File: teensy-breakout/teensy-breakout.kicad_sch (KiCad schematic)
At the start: 1 part, among them U1 Teensy4.1

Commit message: Initial work on teensy brakeout PCB
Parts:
- added C1, C2: 100u, symbol Device:C_Polarized_US
- added C10, C11: C, symbol Device:C
- added C12, C9: 100n, Capacitor_SMD:C_0805_2012Metric, symbol Device:C
- added C13, C3, C5, C7, C8: 10u, Capacitor_SMD:C_0805_2012Metric, symbol Device:C
- added C4, C6: 1u, Capacitor_SMD:C_0805_2012Metric, symbol Device:C
- added CR1: L7805CD2T-TR, Custom:D2PAKSMD_2L_STD-ST_STM, symbol custom:L7805CD2T-TR
- added CR2: MBRD10100CT-13, Custom:TO252DPAK_DIO, symbol custom:MBRD10100CT-13
- added D1, D2: LED, symbol Device:LED
- added J1: USB_B, Connector_USB:USB_B_OST_USB-B1HSxx_Horizontal, symbol Connector:USB_B
- added Q1: IRL530NSTRLPBF, Custom:D2PAKSMD_2L_STD-ST_STM, symbol custom:IRL530NSTRLPBF
- added R1: 1k, Resistor_SMD:R_0805_2012Metric, symbol Device:R_US
- added R2: 10k, Resistor_SMD:R_0805_2012Metric, symbol Device:R_US
- added R3, R4: 270, Resistor_SMD:R_0805_2012Metric, symbol Device:R_US
- added R5, R6: 2k, Resistor_SMD:R_0805_2012Metric, symbol Device:R_US
- added U2: ~, Custom:BNO085, symbol custom:BNO085
- added U3: FT232RL, Package_SO:SSOP-28_5.3x10.2mm_P0.65mm, symbol Interface_USB:FT232RL
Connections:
- net GND: now reaches U1.1 (GND)
- net GND: now also U1.34 (GND), U1.47 (GND), C1.2, C10.2, C11.2, C12.2, C13.2, C2.2, C3.2, C4.2, C5.2, C6.2, C7.2, C8.2, C9.1, CR1.2 (GROUND), J1.4 (GND), J1.5 (Shield), Q1.3 (S), R2.1, U2.3 (GND), U3.18 (GND), U3.21 (GND), U3.25 (AGND), U3.26 (TEST), U3.7 (GND)
- net +3V3: now reaches U1.15 (3V3)
- net +3V3: now also U1.46 (3V3), C11.1, C7.1, R5.1, R6.1, U2.1 (VIN)
- net UART1 RX: now reaches U1.2 (0_RX1_CRX2_CS1)
- net UART1 RX: now also U3.1 (TXD)
- net UART1 TX: now reaches U1.3 (1_TX1_CTX2_MISO1)
- net UART1 TX: now also U3.5 (RXD)
- net UART1 RTS: now reaches U1.4 (2_OUT2)
- net UART1 RTS: now also U3.3 (RTS)
- net I2C0_SDA: now reaches U1.40 (18_A4_SDA)
- net I2C0_SDA: now also R6.2, U2.5 (SDA)
- net I2C0_SCL: now reaches U1.41 (19_A5_SCL)
- net I2C0_SCL: now also R5.2, U2.4 (SCL)
- net +5V: now reaches U1.48 (VIN)
- net +5V: now also C10.1, C12.1, C13.1, C2.1, C5.1, C6.1, C8.1, CR1.3 (OUTPUT), U3.19 (~{RESET}), U3.20 (VCC)
- net UART1 CTS: now reaches U1.5 (3_LRCLK2)
- net UART1 CTS: now also U3.11 (CTS)
- new net: CR2.1, CR2.3, Q1.2 (D)
- new net: D1.1 (K), U3.23 (CBUS0)
- new net: D1.2 (A), R3.2
- new net: Q1.1 (G), R1.2, R2.2
- new net: C9.2, R3.1, R4.1, U3.17 (3V3OUT), U3.4 (VCCIO)
- new net: D2.1 (K), U3.22 (CBUS1)
- new net: D2.2 (A), R4.2
- new net +12V: C1.1, C3.1, C4.1, CR1.1 (INPUT), CR2.2
- new net USB_DM: J1.2 (D-)
- new net USB_DP: J1.3 (D+)
- no-connect marks 0 -> 18
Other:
- moved on the sheet: U1

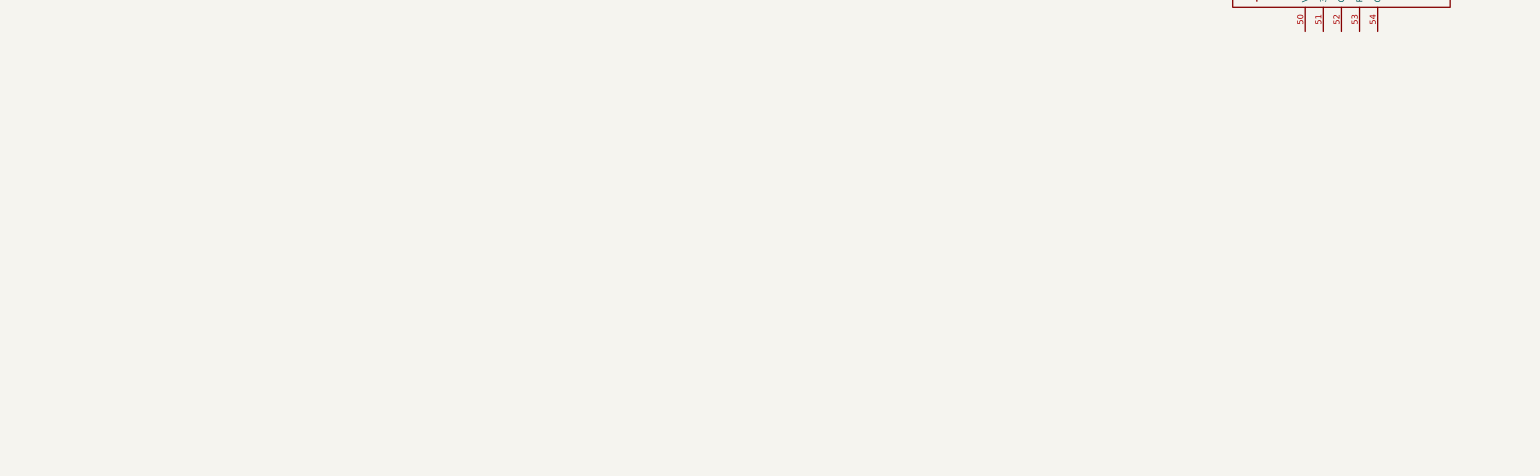
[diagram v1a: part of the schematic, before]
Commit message: Started working to integrate ZED-F9P and feather. Still need to make Zed-F9P footprint.
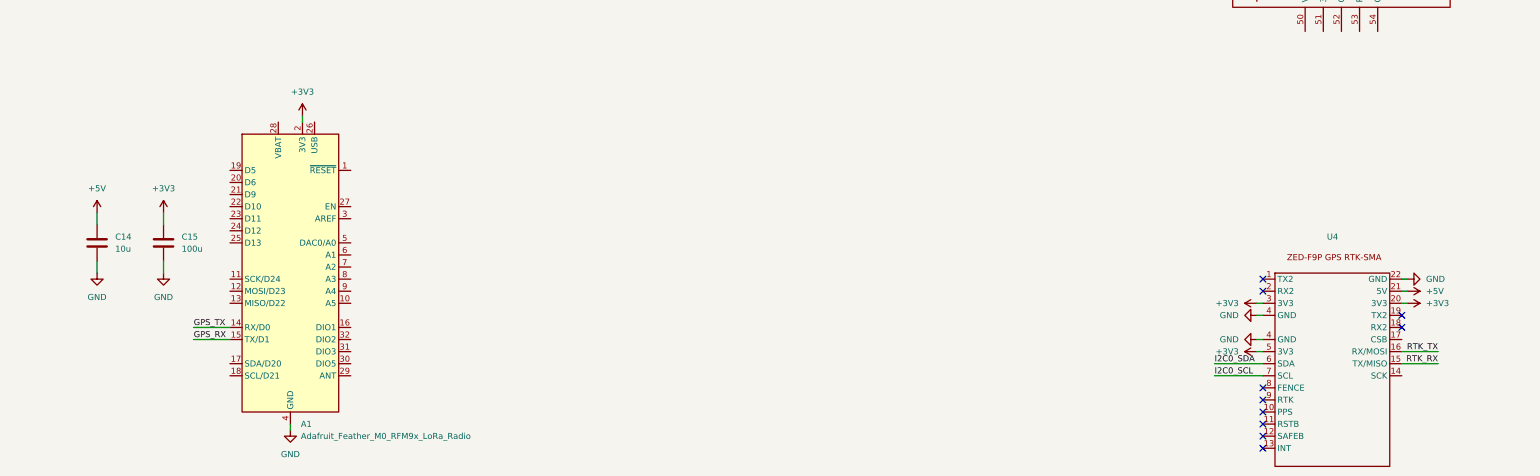
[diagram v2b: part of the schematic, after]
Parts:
- added A1: Adafruit_Feather_M0_RFM9x_LoRa_Radio, Module:Adafruit_Feather_M0_RFM, symbol MCU_Module:Adafruit_Feather_M0_RFM9x_LoRa_Radio
- added C14: 10u, symbol Device:C
- added C15: 100u, symbol Device:C
- added U4: ~, symbol custom:ZED-F9P-GPS-RTK-SMA
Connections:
- net +3V3: now also A1.2 (3V3), C15.2, U4.20 (3V3), U4.3 (3V3), U4.5 (3V3)
- net +5V: now also C14.1, U4.21 (5V)
- net GND: now also A1.4 (GND), C14.2, C15.1, U4.22 (GND), U4.4 (GND)
- net I2C0_SCL: now also U4.7 (SCL)
- net I2C0_SDA: now also U4.6 (SDA)
- new net GPS_RX: A1.15 (TX/D1)
- new net GPS_TX: A1.14 (RX/D0)
- new net RTK_RX: U4.15 (TX/MISO)
- new net RTK_TX: U4.16 (RX/MOSI)
- no-connect marks 18 -> 28

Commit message: More work done on schematic, seems good to me
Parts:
- added C16, C21, C23, C24: 10u, Capacitor_SMD:C_0805_2012Metric_Pad1.18x1.45mm_HandSolder, symbol Device:C
- added C17, C18, C19, C22: 1u, Capacitor_SMD:C_0805_2012Metric_Pad1.18x1.45mm_HandSolder, symbol Device:C
- added C20: 100u, Capacitor_SMD:C_0805_2012Metric_Pad1.18x1.45mm_HandSolder, symbol Device:C
- added D3: LED, LED_SMD:LED_0805_2012Metric_Pad1.15x1.40mm_HandSolder, symbol Device:LED
- added J10, J15, J16, J2, J3, J4, J5, J6, J7: 1988820, Custom:CONN_1988820, symbol custom:1988820
- added J11, J12, J13, J14, J18: 1988817, Custom:CONN_1988817, symbol custom:1988817
- added J17, J21, J9: 1988956, Custom:CONN_1988956, symbol custom:1988956
- added J19, J20: 1989010, Custom:PHOENIX_1989010, symbol custom:1989010
- added J8: 1988833, Custom:CONN_1988833, symbol custom:1988833
- added R10, R9: 10k, Resistor_SMD:R_0805_2012Metric_Pad1.20x1.40mm_HandSolder, symbol Device:R_US
- added R11, R12: 2k, Resistor_SMD:R_0805_2012Metric_Pad1.20x1.40mm_HandSolder, symbol Device:R_US
- added R7: R_US, symbol Device:R_US
- added R8: 1k, Resistor_SMD:R_0805_2012Metric_Pad1.20x1.40mm_HandSolder, symbol Device:R_US
- added SW1: 7101MD9AQE, Custom:SW3_7101MD9AQE_CNK, symbol custom:7101MD9AQE
- added U10, U7: LSF0102DCUR, DCU0008A_N, symbol custom:LSF0102DCUR
- added U5: ~, Custom:RFM69HCW Adafruit Breakout, symbol custom:RFM69HCW_Adafruit_Breakout
- added U6: ICL7667CBAZA-TDKR, Custom:SOIC8_4X5_INR, symbol custom:ICL7667CBAZA-TDKR
- added U9: ICL7667CBAZA-TDKR, Custom:DCU0008A_M, symbol custom:ICL7667CBAZA-TDKR
- C12: value 100n -> 1u; footprint Capacitor_SMD:C_0805_2012Metric -> Capacitor_SMD:C_0805_2012Metric_Pad1.18x1.45mm_HandSolder
- C13, C3, C4, C5, C6, C7, C8, C9: footprint Capacitor_SMD:C_0805_2012Metric -> Capacitor_SMD:C_0805_2012Metric_Pad1.18x1.45mm_HandSolder
- C14: footprint (none) -> Capacitor_SMD:C_0805_2012Metric_Pad1.18x1.45mm_HandSolder
- C15: value 100u -> 1u; footprint (none) -> Capacitor_SMD:C_0805_2012Metric_Pad1.18x1.45mm_HandSolder
- R3, R4, R5, R6: footprint Resistor_SMD:R_0805_2012Metric -> Resistor_SMD:R_0805_2012Metric_Pad1.20x1.40mm_HandSolder
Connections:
- net RTK_RX is gone; now on net GPS_TX: U4.15 (TX/MISO)
- net RTK_TX is gone; now on net GPS_RX: U4.16 (RX/MOSI)
- net +12V: now also J9.2, R8.1
- net +3V3: now also C14.1, C17.2, C19.1, C20.1, C21.1, C22.1, C24.1, J16.1, J4.1, J4.2, J4.3, J4.4, J5.1, J5.2, J5.3, J5.4, R10.1, R11.1, R12.1, R7.2, R9.1, U10.2 (VREF_A), U5.1 (VIN), U7.2 (VREF_A), U9.3 (V-)
- net +5V: now also C16.1, C18.1, C23.1, J11.1, J12.1, J13.1, J14.1, J15.1, J6.1, J6.2, J6.3, J6.4, J7.1, J7.2, J7.3, J7.4, J8.4, J8.5, SW1.1, U10.7 (VREF_B), U10.8 (EN), U6.6 (V+), U7.7 (VREF_B), U7.8 (EN), U9.6 (V+); no longer C14.1, CR1.3 (OUTPUT)
- net GND: now also C16.2, C17.1, C18.2, C19.2, C20.2, C21.2, C22.2, C23.2, C24.2, J10.1, J10.2, J11.3, J12.3, J13.3, J14.3, J15.4, J16.4, J2.1, J2.2, J2.3, J2.4, J3.1, J3.2, J3.3, J3.4, U10.1 (GND), U5.2 (GND), U6.3 (V-), U7.1 (GND)
- net at CR2.1, CR2.3, Q1.2 (D): now also D3.1 (K), J9.1
- net BRAKE: now reaches R1.1
- net BRAKE: now also U1.18 (26_A12_MOSI1)
- net RC_TX: now reaches U1.10 (8_TX2_IN1)
- net RC_TX: now also U9.4 (INB)
- net NP4: now reaches U1.11 (9_OUT1C)
- net NP4: now also U7.4 (A2)
- net RF_CS: now reaches U1.12 (10_CS_MQSR)
- net RF_CS: now also U5.8 (CS)
- net MOSI: now reaches U1.13 (11_MOSI_CTX1)
- net MOSI: now also J18.1, U5.7 (MOSI)
- net MISO: now reaches U1.14 (12_MISO_MQSL)
- net MISO: now also J18.2, U5.6 (MISO)
- net J0_1: now reaches U1.16 (24_A10_TX6_SCL2)
- net J0_1: now also J19.1
- net J0_2: now reaches U1.17 (25_A11_RX6_SDA2)
- net J0_2: now also J19.2
- net PUL: now reaches U1.19 (27_A13_SCK1)
- net PUL: now also J16.2, U6.2 (INA)
- net J0_3: now reaches U1.20 (28_RX7)
- net J0_3: now also J19.3
- net J0_4: now reaches U1.21 (29_TX7)
- net J0_4: now also J19.4
- net J0_5: now reaches U1.22 (30_CRX3)
- net J0_5: now also J19.5
- net J0_6: now reaches U1.23 (31_CTX3)
- net J0_6: now also J19.6
- net J0_7: now reaches U1.24 (32_OUT1B)
- net J0_7: now also J19.7
- net J0_8: now reaches U1.25 (33_MCLK2)
- net J0_8: now also J19.8
- net J1_1: now reaches U1.26 (34_RX8)
- net J1_1: now also J20.1
- net J1_2: now reaches U1.27 (35_TX8)
- net J1_2: now also J20.2
- net RF_G0: now reaches U1.28 (36_CS)
- net RF_G0: now also U5.4 (G0)
- net RF_RST: now reaches U1.29 (37_CS)
- net RF_RST: now also U5.9 (RST)
- net DIR: now reaches U1.30 (38_CS1_IN1)
- net DIR: now also J16.3, U6.4 (INB)
- net ALM: now reaches U1.31 (39_MISO1_OUT1A)
- net ALM: now also J8.1, R7.1
- net J1_3: now reaches U1.32 (40_A16)
- net J1_3: now also J20.3
- net J1_4: now reaches U1.33 (41_A17)
- net J1_4: now also J20.4
- net SCK: now reaches U1.35 (13_SCK_LED)
- net SCK: now also J18.3, U5.5 (SCK)
- net J1_5: now reaches U1.36 (14_A0_TX3_SPDIF_OUT)
- net J1_5: now also J20.5
- net J1_6: now reaches U1.37 (15_A1_RX3_SPDIF_IN)
- net J1_6: now also J20.6
- net at U1.38 (16_A2_RX4_SCL1): now also J17.2, R12.2
- net at U1.39 (17_A3_TX4_SDA1): now also J17.1, R11.2
- net J1_7: now reaches U1.42 (20_A6_TX5_LRCLK1)
- net J1_7: now also J20.7
- net J1_8: now reaches U1.43 (21_A7_RX5_BCLK1)
- net J1_8: now also J20.8
- net J2_1: now reaches U1.44 (22_A8_CTX1)
- net J2_1: now also J21.1
- net J2_2: now reaches U1.45 (23_A9_CRX1_MCLK1)
- net J2_2: now also J21.2
- net NP1: now reaches U1.6 (4_BCLK2)
- net NP1: now also U10.3 (A1)
- net NP2: now reaches U1.7 (5_IN2)
- net NP2: now also U10.4 (A2)
- net NP3: now reaches U1.8 (6_OUT1D)
- net NP3: now also U7.3 (A1)
- net RC_RX: now reaches U1.9 (7_RX2_OUT1A)
- net RC_RX: now also U9.2 (INA)
- new net: D3.2 (A), R8.2
- new net: J11.2, U10.6 (B1)
- new net: J15.2, U9.7 (OUTA)
- new net: J15.3, U9.5 (OUTB)
- new net: J13.2, U7.6 (B1)
- new net: J12.2, U10.5 (B2)
- new net: CR1.3 (OUTPUT), SW1.2
- new net: J14.2, U7.5 (B2)
- new net DIR_MIN: J8.2, U6.5 (OUTB)
- new net LIM_L: J10.4, R9.2
- new net LIM_R: J10.3, R10.2
- new net PUL_MIN: J8.3, U6.7 (OUTA)
- no-connect marks 28 -> 32

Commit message: Forgot to add power LED
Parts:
- added D4: LED, symbol Device:LED
- added R13: R_US, symbol Device:R_US
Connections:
- net +5V: now also D4.2 (A)
- net GND: now also R13.2
- new net: D4.1 (K), R13.1

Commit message: Work on layout & wiring. Mostly done, need to look it over. It's very messy :(
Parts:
- removed J16: 1988820, Custom:CONN_1988820, symbol custom:1988820
- removed U9: ICL7667CBAZA-TDKR, Custom:DCU0008A_M, symbol custom:ICL7667CBAZA-TDKR
- added C25: 1u, Capacitor_SMD:C_0805_2012Metric_Pad1.18x1.45mm_HandSolder, symbol Device:C
- added CR3, CR4: L7805CD2T-TR, Custom:D2PAKSMD_2L_STD-ST_STM, symbol custom:L7805CD2T-TR
- added J22: 1988817, Custom:CONN_1988817, symbol custom:1988817
- added R14, R15, R16: 200k, Resistor_SMD:R_0805_2012Metric_Pad1.20x1.40mm_HandSolder, symbol Device:R_US
- added U8: LSF0102DCUR, Custom:DCU0008A_M, symbol custom:LSF0102DCUR
- C1, C2: footprint (none) -> Custom:CAP_A765EB_KEM
- C20: value 100u -> 1u
- D1, D2: value LED -> BLUE; footprint (none) -> LED_SMD:LED_0805_2012Metric
- D4: value LED -> GREEN; footprint (none) -> LED_SMD:LED_0805_2012Metric
- R13: value R_US -> 120; footprint (none) -> Resistor_SMD:R_0805_2012Metric_Pad1.20x1.40mm_HandSolder
- R7: value R_US -> 500; footprint (none) -> Resistor_SMD:R_0805_2012Metric_Pad1.20x1.40mm_HandSolder
- U10, U7: footprint DCU0008A_N -> Custom:DCU0008A_M
- U4: footprint (none) -> Custom:ZED F9P RTK SMA
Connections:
- net +12V: now also J21.1, CR3.1 (INPUT), CR4.1 (INPUT)
- net +3V3: now also C16.1, U4.21 (3V3), U4.6 (3V3), U8.2 (VREF_A); no longer U4.20 (3V3), U4.5 (3V3)
- net +5V: now also U4.22 (5V), C25.1, R14.1; no longer C16.1, J11.1, J12.1, J13.1, J14.1, J6.1, J6.2, J6.3, J6.4, J7.1, J7.2, J7.3, J7.4, U10.7 (VREF_B), U10.8 (EN), U4.21 (5V), U7.7 (VREF_B), U7.8 (EN)
- net ALM: now also U1.43 (21_A7_RX5_BCLK1); no longer U1.31 (39_MISO1_OUT1A)
- net BRAKE: now also U1.44 (22_A8_CTX1); no longer U1.18 (26_A12_MOSI1)
- net GND: now also J21.2, U4.23 (GND), U4.5 (GND), C25.2, CR3.2 (GROUND), CR4.2 (GROUND), U8.1 (GND); no longer U4.22 (GND)
- net GPS_RX: now also U4.17 (RX/MOSI); no longer U4.16 (RX/MOSI)
- net GPS_TX: now also U4.16 (TX/MISO); no longer U4.15 (TX/MISO)
- net I2C0_SCL: now also U4.8 (SCL); no longer U4.7 (SCL)
- net I2C0_SDA: now also U4.7 (SDA); no longer U4.6 (SDA)
- net PUL: now also U1.45 (23_A9_CRX1_MCLK1); no longer U1.19 (27_A13_SCK1)
- net RC_RX: now also U8.3 (A1)
- net RC_TX: now also U8.4 (A2)
- net USB_DM: now also U3.16 (USBD-)
- net USB_DP: now also U3.15 (USBD+)
- net at J15.2: now also U8.6 (B1)
- net at J15.3: now also U8.5 (B2)
- net J1_8: no longer names the net of J20.8
- net J1_8: no longer U1.43 (21_A7_RX5_BCLK1)
- removed net J2_1: J21.1, U1.44 (22_A8_CTX1)
- removed net J2_2: J21.2, U1.45 (23_A9_CRX1_MCLK1)
- net MISO renamed MISO0
- net MOSI renamed MOSI0
- net SCK renamed SCK0
- new net: CR4.3 (OUTPUT), J11.1, J12.1, J13.1, J14.1, R15.1, R16.1
- new net: CR3.3 (OUTPUT), J6.1, J6.2, J6.3, J6.4, J7.1, J7.2, J7.3, J7.4
- new net: R16.2, U7.7 (VREF_B), U7.8 (EN)
- new net: R15.2, U10.7 (VREF_B), U10.8 (EN)
- new net: R14.2, U8.7 (VREF_B), U8.8 (EN)
- new net MISO1: J22.2, U1.31 (39_MISO1_OUT1A)
- new net MOSI1: J22.1, U1.18 (26_A12_MOSI1)
- new net SCK1: J22.3, U1.19 (27_A13_SCK1)
- no-connect marks 32 -> 83
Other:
- moved on the sheet: J6, J7

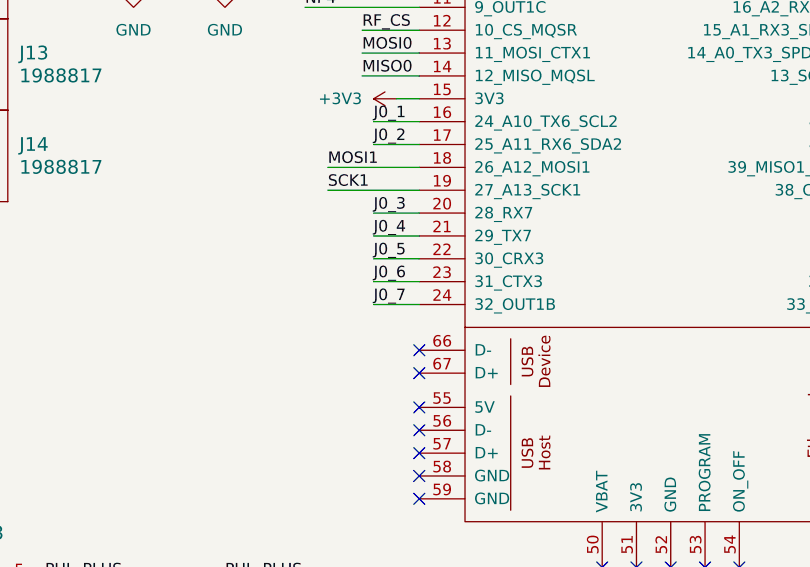
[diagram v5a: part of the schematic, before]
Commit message: Added connection for limit switches, started work on adding headers
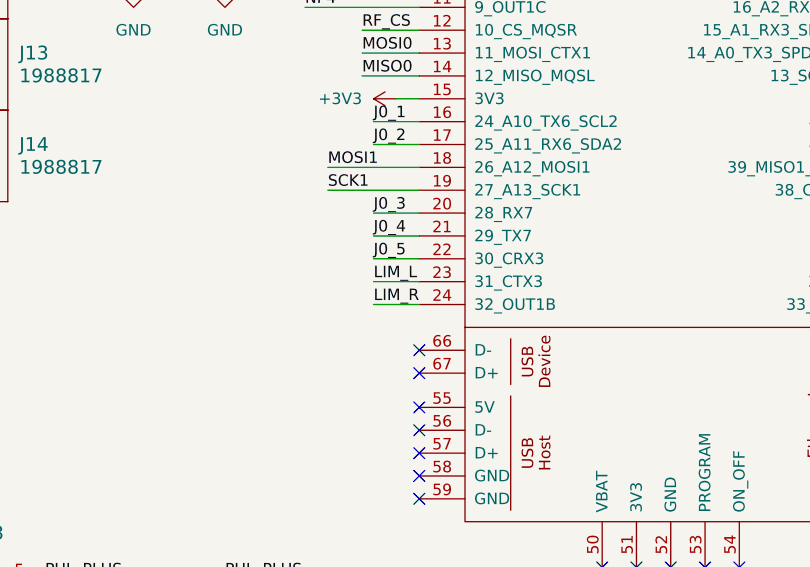
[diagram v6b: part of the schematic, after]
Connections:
- net J0_6: no longer U1.23 (31_CTX3)
- net J0_7: no longer U1.24 (32_OUT1B)
- net LIM_L: now also U1.23 (31_CTX3)
- net LIM_R: now also U1.24 (32_OUT1B)
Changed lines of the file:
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@@
 		)
 	)
-	(label "J0_6"
+	(label "LIM_L"
 		(at 402.59 100.33 0)
 		(fields_autoplaced yes)
@@
 		)
 	)
-	(label "J0_7"
+	(label "LIM_R"
 		(at 402.59 102.87 0)
 		(fields_autoplaced yes)

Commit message: Improved schematic layout, still in  progress
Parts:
- removed C10, C11: C, symbol Device:C
- removed CR1, CR3, CR4: L7805CD2T-TR, Custom:D2PAKSMD_2L_STD-ST_STM, symbol custom:L7805CD2T-TR
- removed J10, J15, J2, J3, J4, J5, J6, J7: 1988820, Custom:CONN_1988820, symbol custom:1988820
- removed J11, J12, J13, J14, J18, J22: 1988817, Custom:CONN_1988817, symbol custom:1988817
- removed J17, J21, J9: 1988956, Custom:CONN_1988956, symbol custom:1988956
- removed J19, J20: 1989010, Custom:PHOENIX_1989010, symbol custom:1989010
- removed J8: 1988833, Custom:CONN_1988833, symbol custom:1988833
- added J10, J11, J14, J15, J4, J5, J6, J7, J8, J9: Conn_01x04, symbol Connector_Generic:Conn_01x04
- added J12: Conn_01x05, symbol Connector_Generic:Conn_01x05
- added J13, J19, J20, J21, J22: Conn_01x03, symbol Connector_Generic:Conn_01x03
- added J16: 1988956, Custom:CONN_1988956, symbol custom:1988956
- added J17, J18: Conn_01x08, symbol Connector_Generic:Conn_01x08
- added J2, J3: Conn_01x02, symbol Connector_Generic:Conn_01x02
- added R17: 1k, Resistor_SMD:R_0805_2012Metric_Pad1.20x1.40mm_HandSolder, symbol Device:R_US
- added U9: ~, symbol custom:D36V50Fx
- CR2: footprint Custom:TO252DPAK_DIO -> TO252DPAK_DIO
- Q1: footprint Custom:D2PAKSMD_2L_STD-ST_STM -> IRL530NSTRLPBF_INF
- U10, U7, U8: footprint Custom:DCU0008A_M -> DCU0008A_N
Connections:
- net J0_8 is gone; now on net J0_6: U1.25 (33_MCLK2)
- net +12V: now also R17.1, U9.11 (VRP), U9.5 (VRP)
- net +3V3: now also J17.7 (Pin_7), J6.1 (Pin_1), J6.2 (Pin_2), J6.3 (Pin_3), J6.4 (Pin_4), J7.1 (Pin_1), J7.2 (Pin_2), J7.3 (Pin_3), J7.4 (Pin_4)
- net +5V: now also R16.1, J10.1 (Pin_1), J12.4 (Pin_4), J12.5 (Pin_5), J19.1 (Pin_1), J20.1 (Pin_1), J21.1 (Pin_1), J22.1 (Pin_1), J8.1 (Pin_1), J8.2 (Pin_2), J8.3 (Pin_3), J8.4 (Pin_4), J9.1 (Pin_1), J9.2 (Pin_2), J9.3 (Pin_3), J9.4 (Pin_4)
- net ALM: now also J12.1 (Pin_1)
- net DIR_MIN: now also J12.2 (Pin_2)
- net GND: now also J10.4 (Pin_4), J11.1 (Pin_1), J11.2 (Pin_2), J13.3 (Pin_3), J14.4 (Pin_4), J15.4 (Pin_4), J17.8 (Pin_8), J18.8 (Pin_8), J19.3 (Pin_3), J20.3 (Pin_3), J21.3 (Pin_3), J22.3 (Pin_3), J4.1 (Pin_1), J4.2 (Pin_2), J4.3 (Pin_3), J4.4 (Pin_4), J5.1 (Pin_1), J5.2 (Pin_2), J5.3 (Pin_3), J5.4 (Pin_4), U9.2 (GND), U9.3 (GND), U9.8 (GND), U9.9 (GND)
- net J0_1: now also J17.1 (Pin_1)
- net J0_2: now also J17.2 (Pin_2)
- net J0_3: now also J17.3 (Pin_3)
- net J0_4: now also J17.4 (Pin_4)
- net J0_5: now also J17.5 (Pin_5)
- net J0_6: now also J17.6 (Pin_6)
- net J1_1: now also J18.1 (Pin_1)
- net J1_2: now also J18.2 (Pin_2)
- net J1_3: now also J18.3 (Pin_3)
- net J1_4: now also J18.4 (Pin_4)
- net J1_5: now also J18.5 (Pin_5)
- net J1_6: now also J18.6 (Pin_6)
- net J1_7: now also J18.7 (Pin_7)
- net LIM_L: now also J11.4 (Pin_4)
- net LIM_R: now also J11.3 (Pin_3)
- net MISO0: now also J14.2 (Pin_2)
- net MISO1: now also J15.2 (Pin_2)
- net MOSI0: now also J14.1 (Pin_1)
- net MOSI1: now also J15.1 (Pin_1)
- net PUL_MIN: now also J12.3 (Pin_3)
- net SCK0: now also J14.3 (Pin_3)
- net SCK1: now also J15.3 (Pin_3)
- net at CR2.1, CR2.3, D3.1 (K)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: now also J16.2
- net at R15.1: no longer R16.1
- net NP1_5V: now reaches U10.6 (B1)
- net NP1_5V: now also J19.2 (Pin_2)
- net at U8.6 (B1): now also J10.2 (Pin_2)
- net at U8.5 (B2): now also J10.3 (Pin_3)
- net I2C1_SDA: now reaches R11.2, U1.39 (17_A3_TX4_SDA1)
- net I2C1_SDA: now also J13.1 (Pin_1)
- net NP3_5V: now reaches U7.6 (B1)
- net NP3_5V: now also J21.2 (Pin_2)
- net NP2_5V: now reaches U10.5 (B2)
- net NP2_5V: now also J20.2 (Pin_2)
- net at SW1.2: now also U9.1 (VOUT), U9.7 (VOUT)
- net I2C1_SCL: now reaches R12.2, U1.38 (16_A2_RX4_SCL1)
- net I2C1_SCL: now also J13.2 (Pin_2)
- net NP4_5V: now reaches U7.5 (B2)
- net NP4_5V: now also J22.2 (Pin_2)
- new net: J16.1, R17.2
- new net: U9.10 (VIN), U9.4 (VIN)
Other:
- note added: "DIR_PLUS"
- note added: "PUL_PLUS"
- moved on the sheet: A1, C12, C13, C14, C15, C16, C17, C18, C19, C20, C21, C22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

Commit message: Added text description to each of the boxes
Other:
- note added: "3V3 GPIO, I2C1, SPI0, SPI1, power LED"
- note added: "433 MHz radio"
- note added: "5V GPIO"
- note added: "Adafruit Feather (GPS RTK base station correction data)"
- note added: "Brake solenoid control"
- note added: "Closed loop stepper motor control"
- note added: "GPS"
- note added: "IMU"
- note added: "Limit switch connector"
- note added: "Power & ground connectors"
- note added: "Power regulation & filtering caps"
- note added: "Serial communication with RC module for communication with TX12 controller"
- note added: "TODO: confirm the RC system uses 5V logic (pretty sure it uses 3v3)"
- note added: "Teensy"
- note added: "UART <--> USB for communication with computer"
